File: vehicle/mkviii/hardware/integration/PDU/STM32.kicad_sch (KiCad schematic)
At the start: 68 parts, among them J7 CONN_02X03, U1 STM32G441CBTx, U2 MCP23S17_SS, U20 ADC1283, U21 MAX7221xNG, U4 CC56-12SEKWA, U6 MCP2561-E_SN, Y1 Crystal_SMD

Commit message: Fix the STM32 schematic
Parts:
- removed C10, C9: C_30pF, OEM:C_0603_1608Metric, symbol formula:C_30pF
- removed C7: C_0.1uF, OEM:C_0603_1608Metric, symbol formula:C_0.1uF
- removed C8: C_100pF, OEM:C_0603_1608Metric, symbol formula:C_100pF
- removed R23: R_10K, OEM:R_0603, symbol OEM:R_10K
- removed R28: R_100, OEM:R_0603, symbol OEM:R_100
- removed U1: STM32G441CBTx, Package_QFP:LQFP-48_7x7mm_P0.5mm, symbol MCU_ST_STM32G4:STM32G441CBTx
- removed Y1: Crystal_SMD, OEM:Crystal_SMD_FA238, symbol formula:Crystal_SMD
- added C10: C_4.7uF, Capacitor_SMD:C_0603_1608Metric, symbol OEM:C_4.7uF_20-100V_0603
- added C13: C_10nF, Capacitor_SMD:C_0603_1608Metric, symbol OEM:C_10nF_20-100V_0603
- added C14: C_1uF, Capacitor_SMD:C_0603_1608Metric, symbol OEM:C_1uF_20-100V_0603
- added C7, C8, C9: C_0.1uF, Capacitor_SMD:C_0603_1608Metric, symbol OEM:C_0.1uF_0-20V_0603
- added U1: STM32G441KBT6, Package_QFP:LQFP-32_7x7mm_P0.8mm, symbol OEM:U_MCU_STM32G441KBT6_32-LQFP
- D17: footprint OEM:CHIPLED_0805 -> LED_SMD:LED_0805_2012Metric
- R22: footprint OEM:R_0603 -> Resistor_SMD:R_0603_1608Metric
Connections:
- net CAN_RX: now also U1.22 ((FDCAN1_TX/GPIO_EXTI12)PA12)
- net CAN_TX: now also U1.21 ((FDCAN1_RX/GPIO_EXTI11)PA11)
- net COOLING_EN: now also U1.10 ((TIM2_ETR/TIM2_CH1/GPIO_EXTI5/ADC2_IN13)PA5*)
- net CS_ADC: now also U1.29 ((TIM4_CH1/TIM16_CH1N/GPIO_EXTI6)PB6)
- net CS_DISP: now also U1.28 ((TIM17_CH1/SPI1_MOSI/TIM3_CH2/TIM16_BKIN/GPIO_EXTI5)PB5)
- net CS_IO: now also U1.30 ((TIM3_CH4/TIM4_CH2/TIM17_CH1N/GPIO_EXTI7)PB7)
- net FAN_PWM: now also U1.8 ((TIM15_CH2/USART2_RX/TIM2_CH4/GPIO_EXTI3/ADC1_IN4)PA3*)
- net GND: now also C10.2, C13.2, C14.2, C7.2, C8.2, C9.2, U1.14 (VSSA), U1.16 (VSS), U1.32 (VSS)
- net HB_LED: now also U1.7 ((TIM15_CH1/USART2_TX/TIM2_CH3/GPIO_EXTI2/ADC1_IN3)PA2*)
- net MISO: now also U1.23 ((SYS_JTMS-SWDIO/GPIO_EXTI13)PA13)
- net MISO_A: now also U1.12 ((TIM3_CH2/TIM17_CH1/GPIO_EXTI7/ADC2_IN4)PA7*)
- net MOSI: now also U1.24 ((SYS_JTCK-SWCLK/GPIO_EXTI14)PA14)
- net MOSI_A: now also U1.13 ((TIM3_CH3/GPIO_EXTI0/ADC1_IN15)PB0*)
- net PUMP_PWM: now also U1.9 ((USART2_CK/TIM3_CH2/GPIO_EXTI4/ADC2_IN17)PA4*)
- net RESET_IO: now also U1.31 ((TIM4_CH3/TIM16_CH1/GPIO_EXTI8)PB8-BOOT0)
- net SCK: now also U1.5 ((TIM2_ETR/TIM2_CH1/GPIO_EXTI0/ADC2_IN1/ADC1_IN1)PA0*)
- net SCK_A: now also U1.6 ((TIM15_CH1N/TIM2_CH2/GPIO_EXTI1/ADC2_IN2/ADC1_IN2)PA1*)
- net SS_ESTOP_L: now also U1.20 ((TIM2_CH4/USART1_RX/TIM17_BKIN/GPIO_EXTI10)PA10)
- net SS_ESTOP_R: now also U1.25 ((TIM2_ETR/TIM2_CH1/GPIO_EXTI15)PA15)
- net SS_GLVMS: now also U1.26 ((TIM3_ETR/SPI1_SCK/TIM4_ETR/TIM2_CH2/GPIO_EXTI3)PB3)
- net SS_MC: now also U1.11 ((TIM3_CH1/TIM16_CH1/GPIO_EXTI6/ADC2_IN3)PA6*)
- net TS_STATUS_G: now also U1.18 ((TIM4_ETR/USART1_CK/GPIO_EXTI8)PA8)
- net TS_STATUS_R: now also U1.19 ((TIM2_CH3/TIM15_BKIN/USART1_TX/GPIO_EXTI9)PA9)
- new net: C10.1, C8.1, C9.1, U1.1 (VDD), U1.17 (VDD)
- new net: C13.1, C14.1, U1.15 (VDDA)
- new net: C7.1, U1.4 ((GPIO_EXTI10)PG10-NRST)
- no-connect marks 13 -> 15
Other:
- moved on the sheet: D17, J7, R21, R22, U21, U4

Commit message: Fix missing 3.3V and reorder some pins
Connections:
- net FAN_PWM: now also U1.7 ((TIM15_CH1/USART2_TX/TIM2_CH3/GPIO_EXTI2/ADC1_IN3)PA2*); no longer U1.8 ((TIM15_CH2/USART2_RX/TIM2_CH4/GPIO_EXTI3/ADC1_IN4)PA3*)
- net HB_LED: now also U1.9 ((USART2_CK/TIM3_CH2/GPIO_EXTI4/ADC2_IN17)PA4*); no longer U1.7 ((TIM15_CH1/USART2_TX/TIM2_CH3/GPIO_EXTI2/ADC1_IN3)PA2*)
- net PUMP_PWM: now also U1.8 ((TIM15_CH2/USART2_RX/TIM2_CH4/GPIO_EXTI3/ADC1_IN4)PA3*); no longer U1.9 ((USART2_CK/TIM3_CH2/GPIO_EXTI4/ADC2_IN17)PA4*)
- net +3.3V: now reaches C10.1, C8.1, C9.1, U1.1 (VDD), U1.17 (VDD)
- net +3.3V: now also C13.1, C14.1, U1.15 (VDDA)
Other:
- moved on the sheet: C10, C8, C9

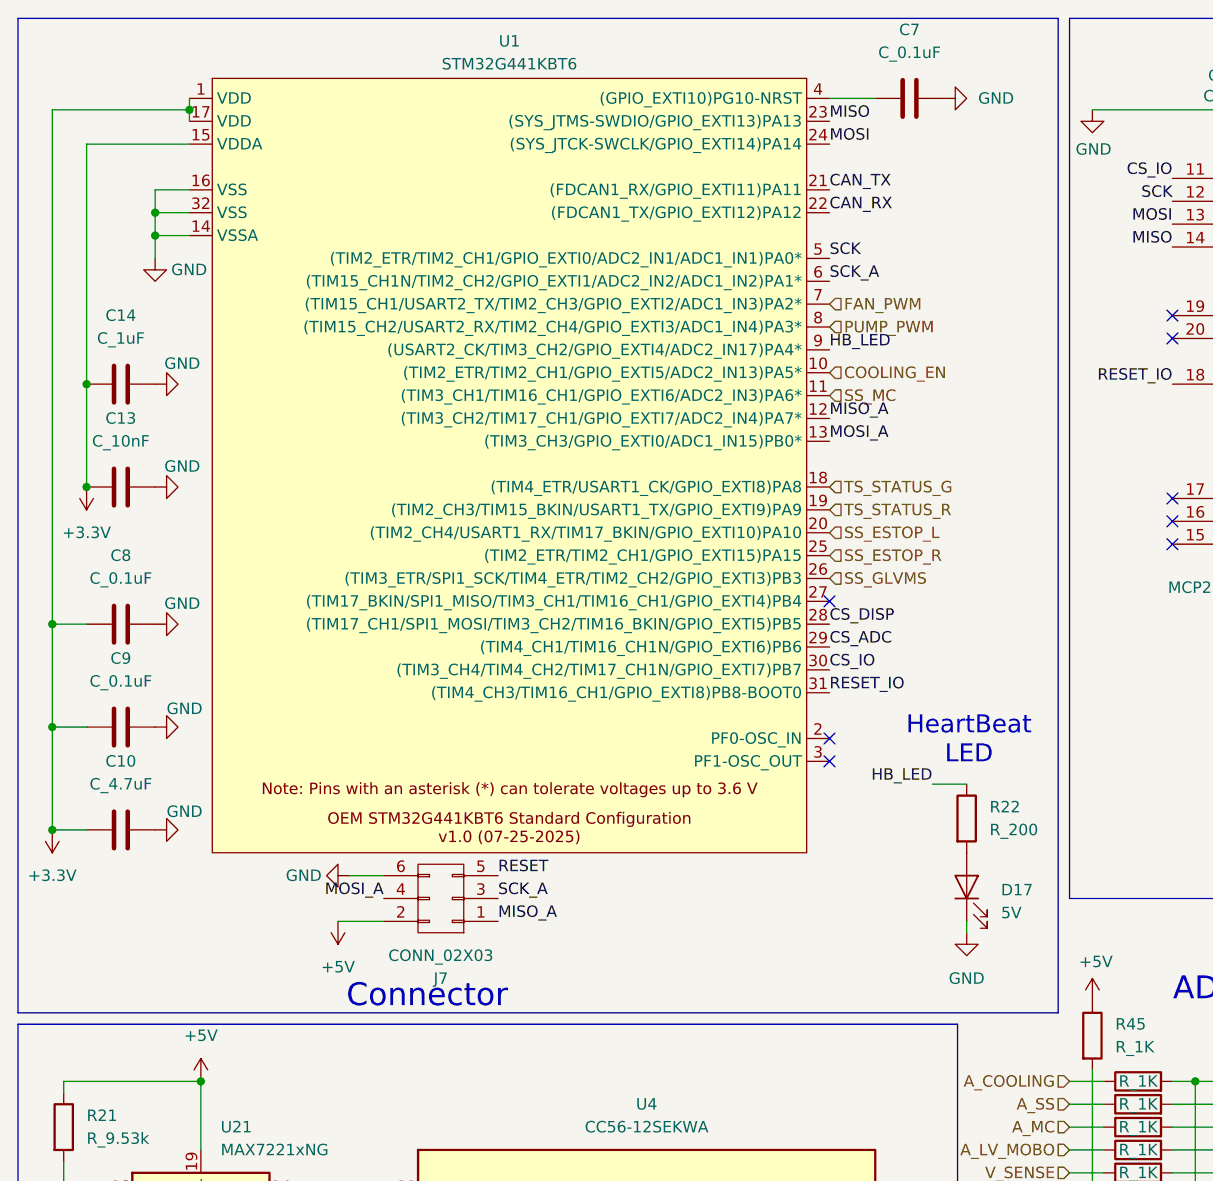
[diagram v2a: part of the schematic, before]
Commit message: Update programming pins and clock oscillator
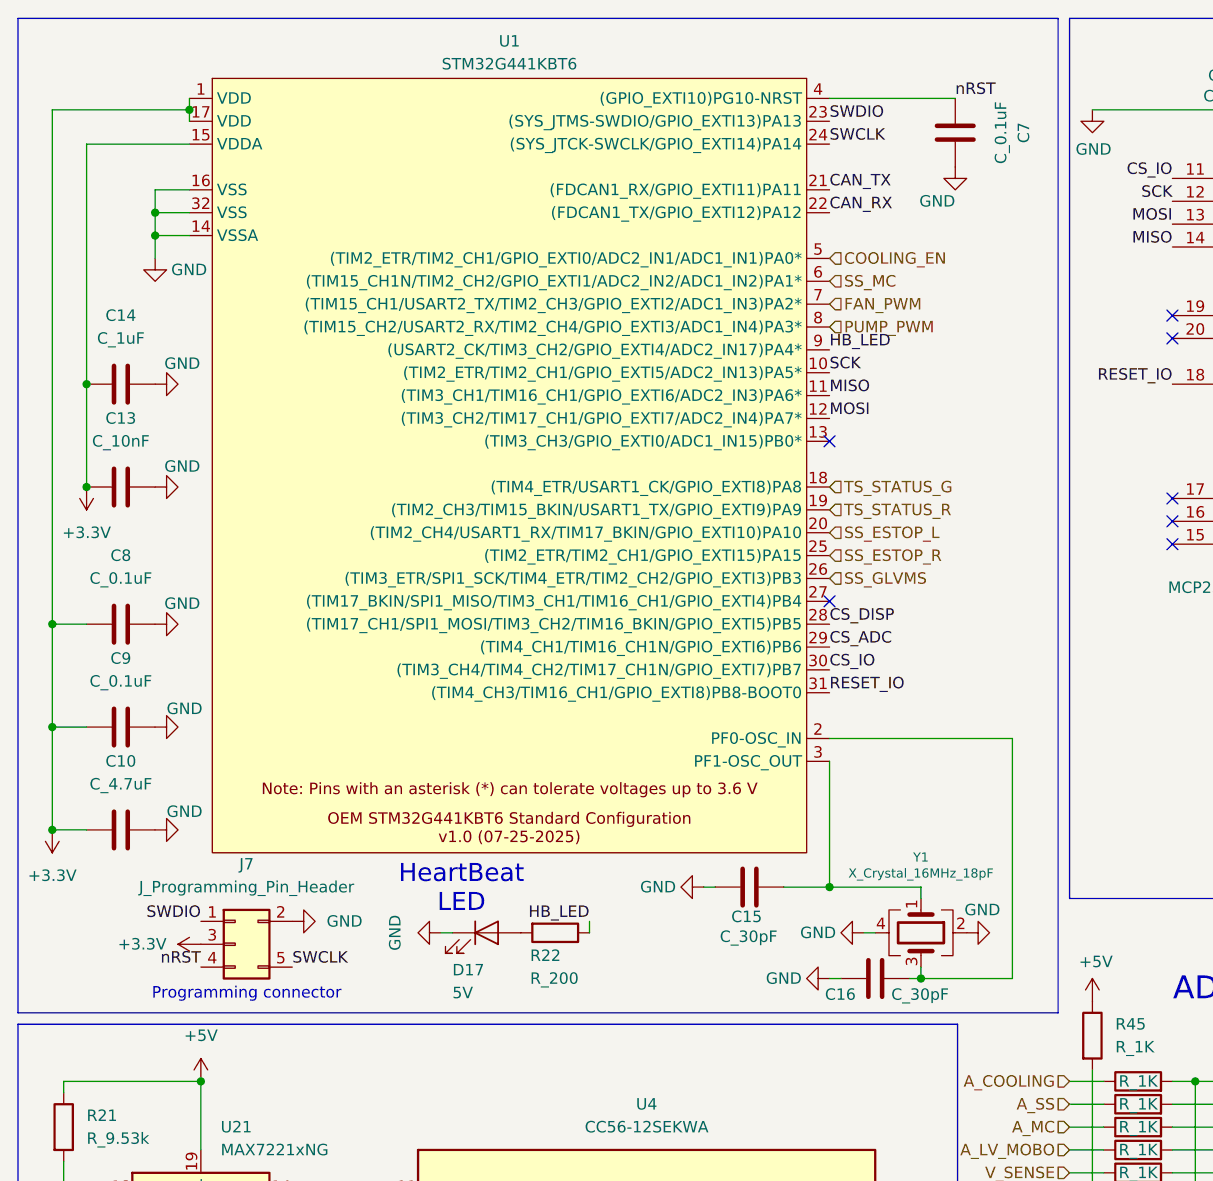
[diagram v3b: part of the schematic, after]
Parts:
- removed J7: CONN_02X03, Connector_PinHeader_2.54mm:PinHeader_2x03_P2.54mm_Vertical, symbol oem:CONN_02X03
- added C15, C16: C_30pF, OEM:C_0603, symbol OEM:C_30pF
- added J7: J_Programming_Pin_Header, OEM:J_Programming_Pin_Header_Keyed, symbol OEM:J_Programming_Pin_Header
- added Y1: X_Crystal_16MHz_18pF, OEM:Crystal_TXC7M, symbol OEM:X_Crystal_16MHz_18pF
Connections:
- net MISO_A is gone; now on net MOSI: U1.12 ((TIM3_CH2/TIM17_CH1/GPIO_EXTI7/ADC2_IN4)PA7*)
- net SCK_A is gone; now on net SS_MC: U1.6 ((TIM15_CH1N/TIM2_CH2/GPIO_EXTI1/ADC2_IN2/ADC1_IN2)PA1*)
- net +3.3V: now also J7.3 (Pin_3)
- net COOLING_EN: now also U1.5 ((TIM2_ETR/TIM2_CH1/GPIO_EXTI0/ADC2_IN1/ADC1_IN1)PA0*); no longer U1.10 ((TIM2_ETR/TIM2_CH1/GPIO_EXTI5/ADC2_IN13)PA5*)
- net GND: now also C15.2, C16.2, J7.2 (Pin_2), Y1.2, Y1.4
- net MISO: now also U1.11 ((TIM3_CH1/TIM16_CH1/GPIO_EXTI6/ADC2_IN3)PA6*); no longer U1.23 ((SYS_JTMS-SWDIO/GPIO_EXTI13)PA13)
- net MOSI: no longer U1.24 ((SYS_JTCK-SWCLK/GPIO_EXTI14)PA14)
- net SCK: now also U1.10 ((TIM2_ETR/TIM2_CH1/GPIO_EXTI5/ADC2_IN13)PA5*); no longer U1.5 ((TIM2_ETR/TIM2_CH1/GPIO_EXTI0/ADC2_IN1/ADC1_IN1)PA0*)
- net SS_MC: no longer U1.11 ((TIM3_CH1/TIM16_CH1/GPIO_EXTI6/ADC2_IN3)PA6*)
- net at U1.2 (PF0-OSC_IN): now also C16.1, Y1.3
- net at U1.3 (PF1-OSC_OUT): now also C15.1, Y1.1
- net nRST: now reaches C7.1, U1.4 ((GPIO_EXTI10)PG10-NRST)
- net nRST: now also J7.4 (Pin_4)
- net MOSI_A: no longer names the net of U1.13 ((TIM3_CH3/GPIO_EXTI0/ADC1_IN15)PB0*)
- new net SWCLK: J7.5 (Pin_5), U1.24 ((SYS_JTCK-SWCLK/GPIO_EXTI14)PA14)
- new net SWDIO: J7.1 (Pin_1), U1.23 ((SYS_JTMS-SWDIO/GPIO_EXTI13)PA13)
- no-connect marks 15 -> 14
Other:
- note added: "Programming connector"
- note removed: "Connector"
- moved on the sheet: C7, D17, R22

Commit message: Add another status LED because why not
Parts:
- added D39: 5V, LED_SMD:LED_0805_2012Metric, symbol oem:LED_0805
- added R71: R_200, Resistor_SMD:R_0603_1608Metric, symbol OEM:R_200
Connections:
- net GND: now also D39.1 (K)
- net at U2.28 (GPA7): now also R71.1
- new net: D39.2 (A), R71.2
- no-connect marks 14 -> 13

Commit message: Add 3.3V buck converter
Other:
- added sheet 3V_Buck (3V_Buck.kicad_sch)
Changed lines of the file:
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@@
 		)
 	)
+	(hierarchical_label "3.3V_OUT"
+		(shape input)
+		(at 144.78 93.98 0)
+		(effects
+			(font
+				(size 1.27 1.27)
+			)
+			(justify left)
+		)
+	)
 	(hierarchical_label "SS_MC"
 		(shape input)
@@
 				)
 			)
+		)
+	)
+	(sheet
+		(at 144.78 88.9)
+		(size 12.7 10.16)
+		(exclude_from_sim no)
+		(in_bom yes)
+		(on_board yes)
+		(dnp no)
+		(fields_autoplaced yes)
+		(stroke
+			(width 0.1524)
+			(type solid)
+		)
+		(fill
+			(color 0 0 0 0)
+		)
+		(property "Sheetname" "3V_Buck"
+			(at 144.78 88.1884 0)
+			(show_name no)
+			(do_not_autoplace no)
+			(effects
+				(font
+					(size 1.27 1.27)
+				)
+				(justify left bottom)
+			)
+		)
+		(property "Sheetfile" "3V_Buck.kicad_sch"
+			(at 144.78 99.6446 0)
+			(show_name no)
+			(do_not_autoplace no)
+			(effects
+				(font
+					(size 1.27 1.27)
+				)
+				(justify left top)
+			)
+		)
+		(instances
+			(project "PDU"
+				(path "/f655fa78-2860-41ca-ba0e-06d986d434be/4d828ac3-ffc9-42fb-a576-78e59bc536b1"
+					(page "10")
+				)
+			)

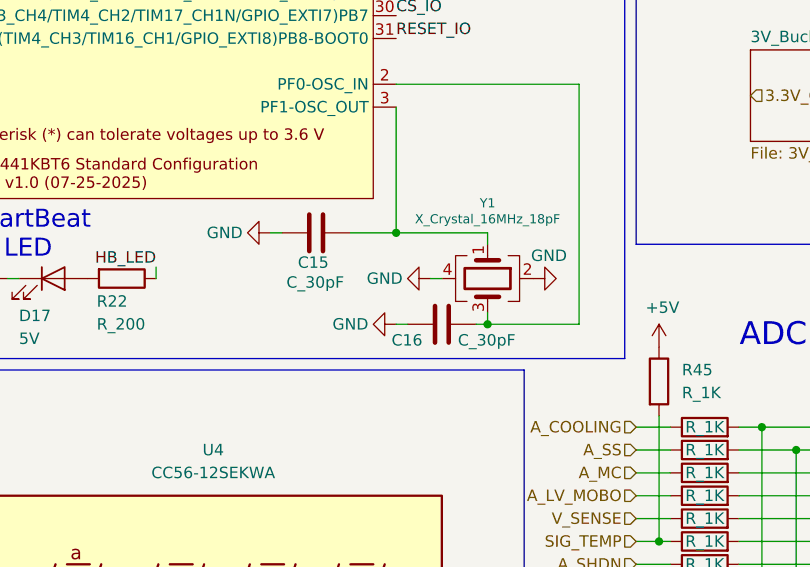
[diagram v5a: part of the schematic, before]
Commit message: Start work on PCB (The parts are placed)
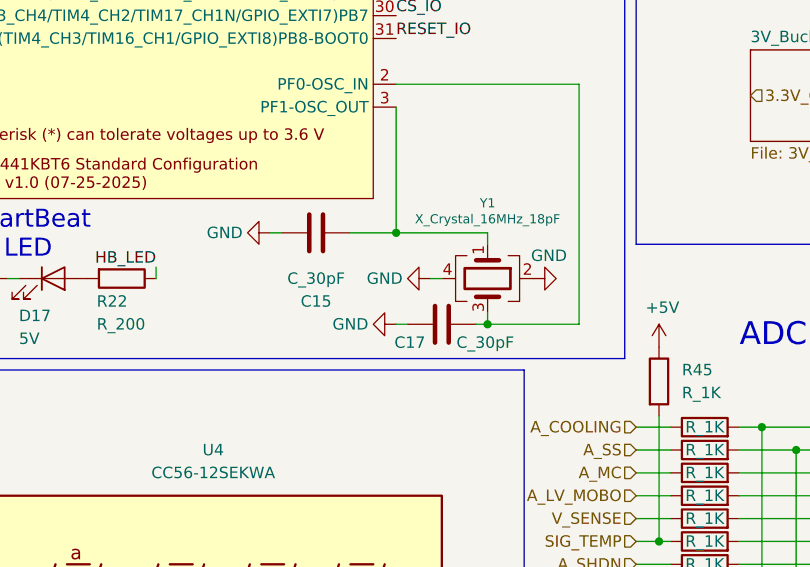
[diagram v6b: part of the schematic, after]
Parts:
- removed C15, C16: C_30pF, OEM:C_0603, symbol OEM:C_30pF
- added C15, C17: C_30pF, Capacitor_SMD:C_0603_1608Metric, symbol OEM:C_30pF_20-100V_0603
- Y1: footprint OEM:Crystal_TXC7M -> Crystal:Crystal_SMD_TXC_7M-4Pin_3.2x2.5mm_HandSoldering
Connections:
- net GND: now also C15.1, C17.1
- net at U1.2 (PF0-OSC_IN), Y1.3: now also C17.2
- net at U1.3 (PF1-OSC_OUT), Y1.1: now also C15.2
